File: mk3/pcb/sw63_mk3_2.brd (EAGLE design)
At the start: 35 x 36 mm, 68 parts, among them J1 USB-C_2.0_SMT, Q1 LGE2305, Q2 N-MOSFET, Q4 TEMT6200FX01, SW1 KSC321JLFS, SW2 EVQ-P7J01P, U1 ATSAMD21E18A-MU, U2 DS3231MZ+, U3 TLC5916IPW, U4 TLC5916IPW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

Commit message: 3_2 update
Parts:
- moved SJ1 0.65 mm to (26.7, 8.81)
- moved B- 0.57 mm to (10.8, 25.3)
- moved SWD 0.30 mm to (16.2, 3.26)
- moved R8 0.17 mm to (11.9, 14.6)
- moved D2 0.16 mm to (20.8, 25.4)
- moved C10 0.13 mm to (11.6, 11.3)
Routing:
- net VBUS_FUSED: track 48.5 -> 30.2 mm, vias 2 -> 0
- net SWCLK: track 6.59 -> 13.8 mm
- net ACTIVE: track 27.8 -> 33.1 mm
- net DCLK: track 0.00 -> 4.80 mm
- net VDD: track 69.5 -> 73.8 mm
- net !RESET: track 77.6 -> 81.7 mm
- net CLK: track 33.5 -> 35.0 mm, vias 4 -> 5
- net SWDIO: track 5.49 -> 6.84 mm
- net GND: track 31.3 -> 31.9 mm, vias 104 -> 116

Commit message: 3_2 update
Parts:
- J1: value USB-C_2.0_SMT -> USB-C_2.0_SMT_WS; device BASTL_CONNECTORS:USB-C_FULL_SMT -> BASTL_CONNECTORS:USB-C_FULL_SMT_WS
- moved J1 2.00 mm to (32.3, 17.5)
- moved D1 0.07 mm to (23.5, 10.00)
- turned PM to 353 degrees
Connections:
- net GND: now also U1.15
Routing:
- net D-: track 18.5 -> 14.4 mm
- net GND: track 31.9 -> 28.6 mm
- net N$2: track 14.3 -> 16.1 mm
- net VDDLEDS: track 111.8 -> 113.0 mm
- net D+: track 15.8 -> 14.7 mm
- net N$1: track 9.34 -> 10.3 mm
- net N$7: track 11.3 -> 10.7 mm
- net VBUS_DTCT: track 40.9 -> 41.5 mm

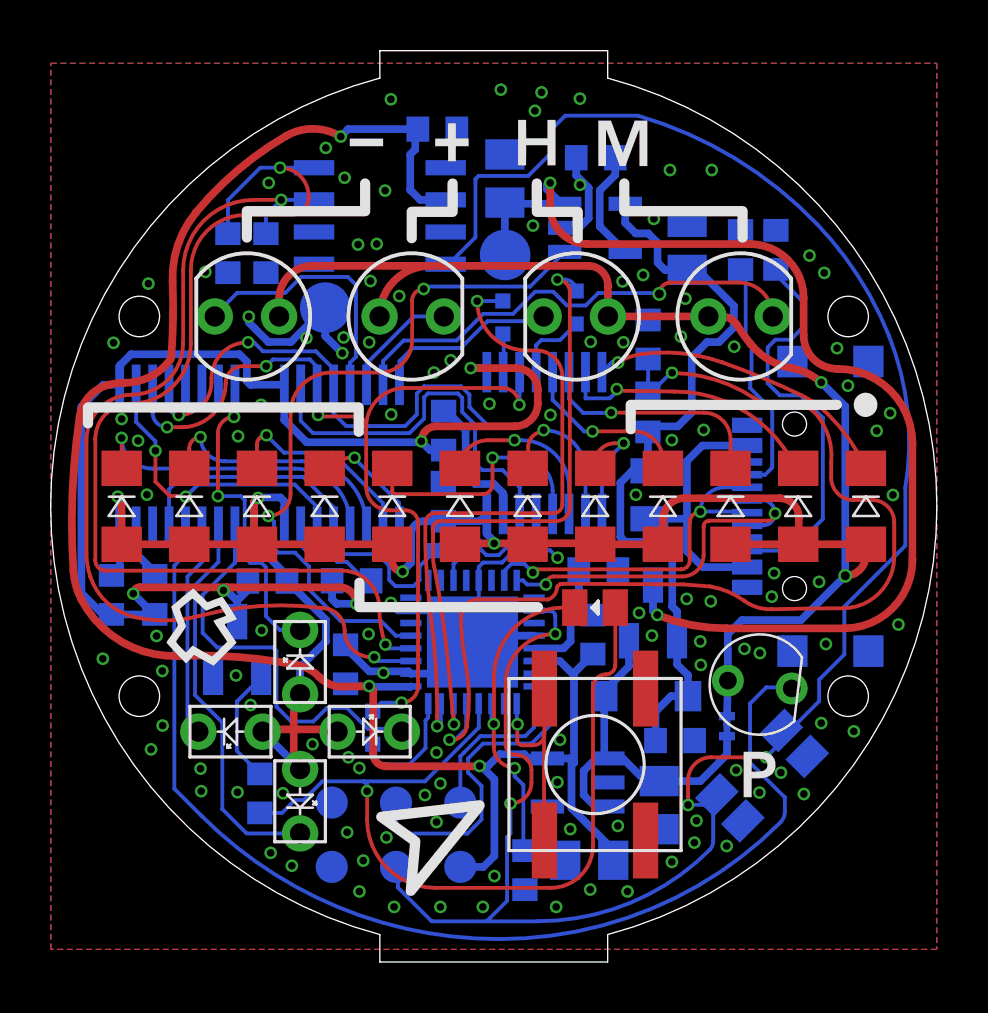
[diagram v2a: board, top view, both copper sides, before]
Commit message: add 3_2 board files
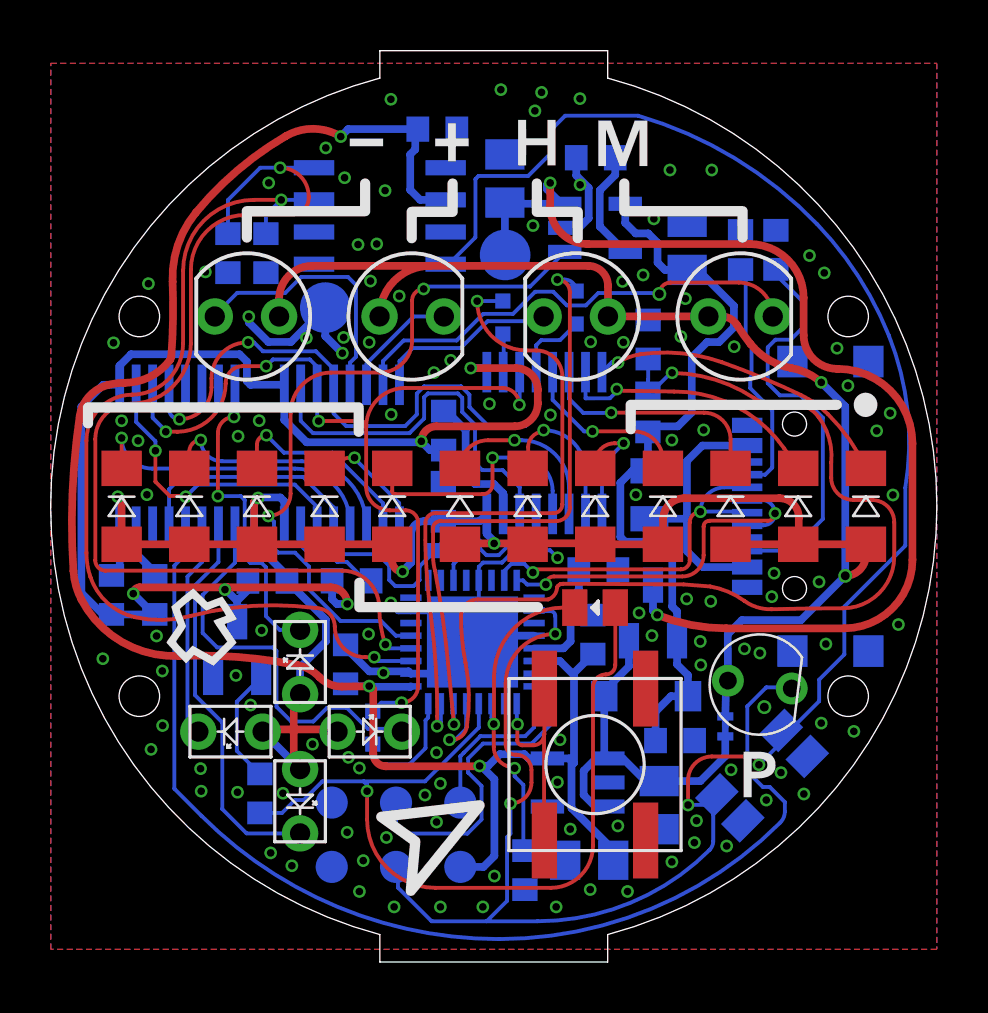
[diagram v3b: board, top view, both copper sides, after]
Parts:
- F1: value 500mA -> BSMD0805-050-24V
- J1: value USB-C_2.0_SMT_WS -> GT-USB-7070C
- Q1: value LGE2305 -> 2305
- Q2: value N-MOSFET -> 2302
- SW2: value EVQ-P7J01P -> TSC4A 160gf-WZ 016
- U6: value MIC5504YM5-TR -> ME6211C33M5G-N
- moved SJ1 0.07 mm to (26.6, 8.81)
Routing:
- net GNDLEDS: track 54.6 -> 53.8 mm
- net GND: vias 116 -> 117
